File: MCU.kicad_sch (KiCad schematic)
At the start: 1 part, among them U1 STM32F030C8T6TR

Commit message: sch done open for review
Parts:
- added C10, C13, C14, C6, C7: 100nF, symbol Device:C_Small
- added C11, C12: 20pF, symbol Device:C_Small
- added C5: 4.7uF, symbol Device:C_Small
- added C8: 1uF, symbol Device:C_Small
- added C9: 10nF, symbol Device:C_Small
- added J2: SWD, symbol Connector:Conn_01x03_Pin
- added R2, R3, R4: 10K, symbol Device:R_Small
- added SW1, SW2, SW3: SW_SPST, symbol Switch:SW_SPST
- added Y1: 8MHZ, symbol Device:Crystal_Small
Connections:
- net VDDA is gone; now on net VCC_3v3: U1.9 (VDDA)
- net VDD__1 is gone; now on net VCC_3v3: U1.24 (VDD__1)
- net VDD__2 is gone; now on net VCC_3v3: U1.48 (VDD__2)
- net VSSA is gone; now on net GND: U1.8 (VSSA)
- net VSS__1 is gone; now on net GND: U1.47 (VSS__1)
- net BOOT0: now also R2.2
- net PA11: now also C13.2, R3.2, SW2.2 (B)
- net PA12: now also C14.2, R4.2, SW3.2 (B)
- net PA13_SWDIO: now also J2.3 (Pin_3)
- net PA14_SWCLK: now also J2.2 (Pin_2)
- net PF0-OSC_IN: now also C12.1, Y1.2
- net PF1-OSC_OUT: now also C11.1, Y1.1
- net ~{RST}: now also C10.2, SW1.2 (B)
- net PA15: no longer names the net of U1.38 (PA15)
- net PB3: no longer names the net of U1.39 (PB3)
- net PB4: no longer names the net of U1.40 (PB4)
- net PB5: no longer names the net of U1.41 (PB5)
- net PB6: no longer names the net of U1.42 (PB6)
- net PB7: no longer names the net of U1.43 (PB7)
- net PB8: no longer names the net of U1.45 (PB8)
- net PB9: no longer names the net of U1.46 (PB9)
- net PC13: no longer names the net of U1.2 (PC13)
- net PC14-OSC32_IN: no longer names the net of U1.3 (PC14-OSC32_IN)
- net PC15-OSC32_OUT: no longer names the net of U1.4 (PC15-OSC32_OUT)
- net PF6: no longer names the net of U1.35 (PF6)
- net PF7: no longer names the net of U1.36 (PF7)
- net VDD renamed VCC_3v3
- net VCC_3v3: now also C5.1, C6.1, C7.1, C8.1, C9.1, R3.1, R4.1
- net VSS renamed GND
- net GND: now also C10.1, C11.2, C12.2, C13.1, C14.1, C5.2, C6.2, C7.2, C8.2, C9.2, J2.1 (Pin_1), R2.1, SW1.1 (A), SW2.1 (A), SW3.1 (A)
- no-connect marks 0 -> 13
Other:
- title: (none) -> Nur-Al-Nujoom

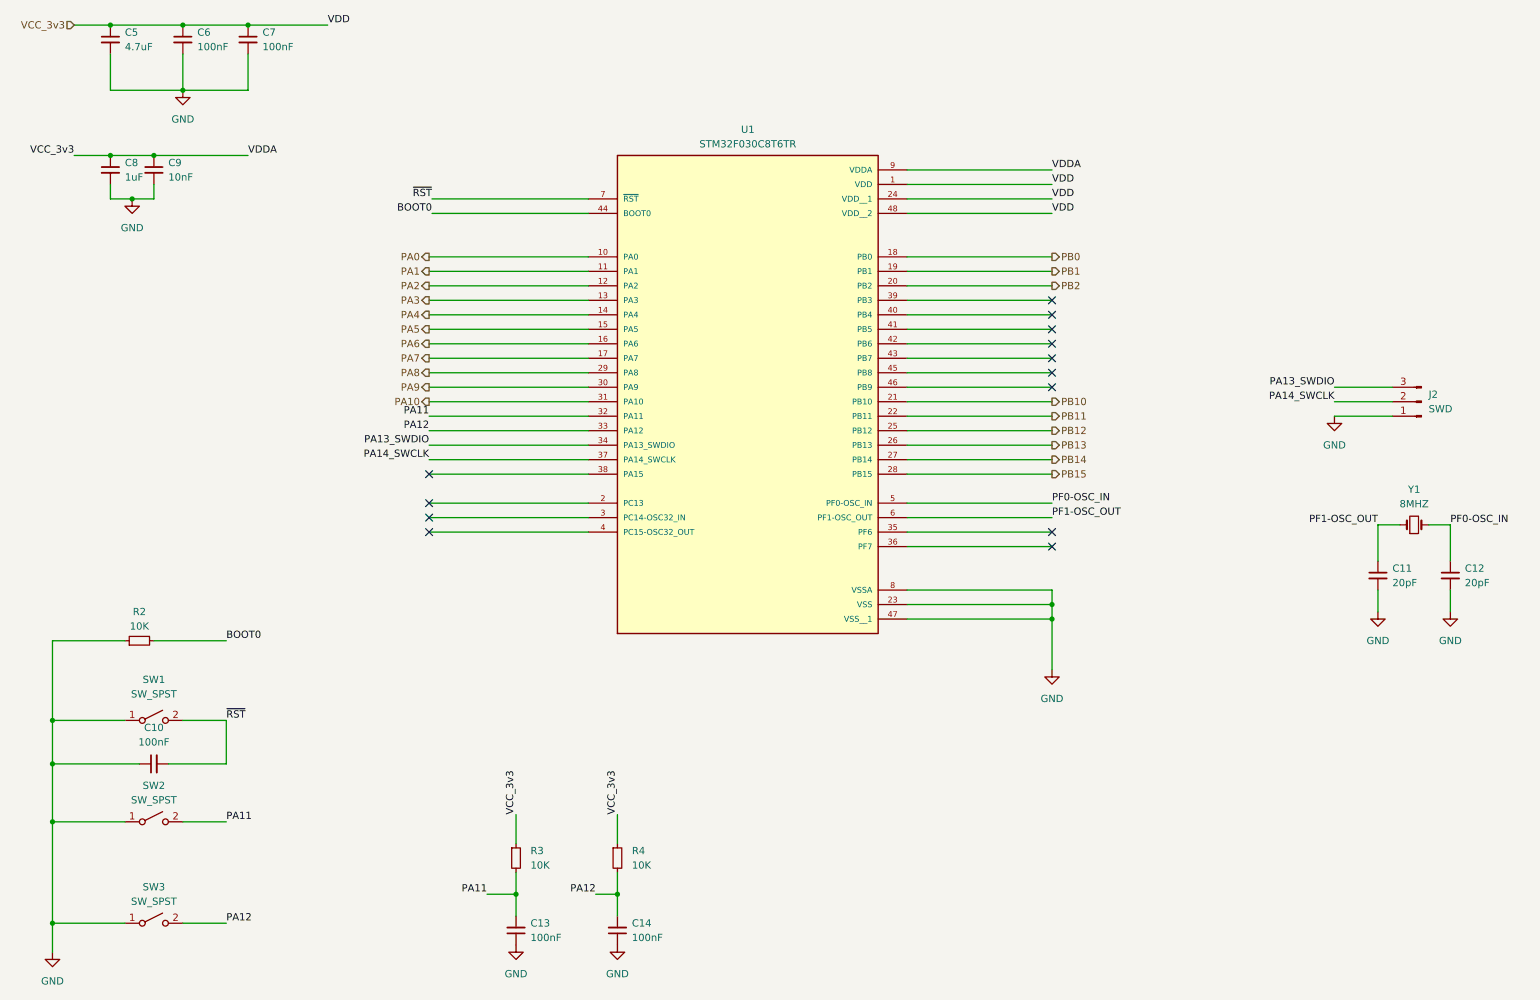
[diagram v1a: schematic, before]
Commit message: updated Routing
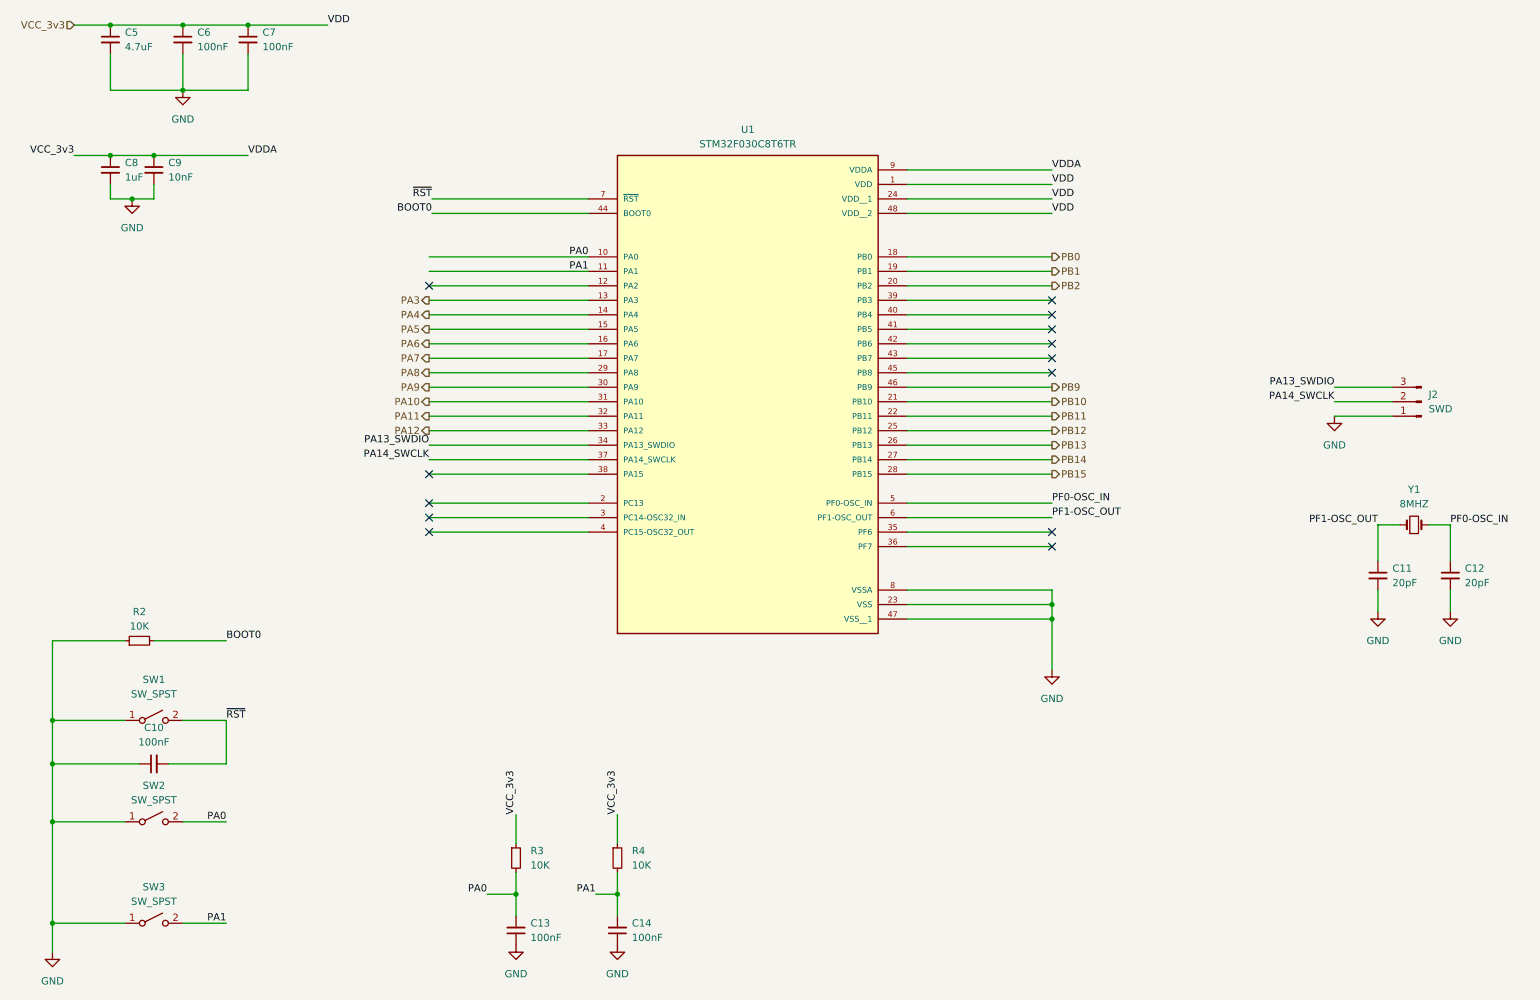
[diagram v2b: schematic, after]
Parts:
- C10, C11, C12, C13, C14, C5, C6, C7, C8, C9: footprint (none) -> Capacitor_SMD:C_0603_1608Metric
- J2: footprint (none) -> Connector_PinHeader_2.54mm:PinHeader_1x03_P2.54mm_Vertical
- R2, R3, R4: footprint (none) -> Resistor_SMD:R_0603_1608Metric
- SW1, SW2, SW3: footprint (none) -> Button_Switch_SMD:SW_SPST_CK_RS282G05A3
- Y1: footprint (none) -> Crystal:Crystal_SMD_HC49-SD
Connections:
- net PA0: now also C13.2, R3.2, SW2.2 (B)
- net PA1: now also C14.2, R4.2, SW3.2 (B)
- net PA11: no longer C13.2, R3.2, SW2.2 (B)
- net PA12: no longer C14.2, R4.2, SW3.2 (B)
- net PB9: now reaches U1.46 (PB9)
- net PA2: no longer names the net of U1.12 (PA2)
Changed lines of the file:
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@@
 	)
 	(no_connect
-		(at 196.85 110.49)
+		(at 87.63 67.31)
 	)
 	(no_connect
-		(at 196.85 80.01)
+		(at 196.85 110.49)
 	)
 	(no_connect
-		(at 196.85 85.09)
+		(at 196.85 80.01)
 	)
 	(no_connect
@@
 		)
 	)
-	(label "VDD"
-		(at 69.85 21.59 0)
-		(fields_autoplaced yes)
+	(label "PA0"
+		(at 115.57 62.23 180)
 		(effects
 			(font
 				(size 1.27 1.27)
 			)
-			(justify left bottom)
+			(justify right bottom)
 		)
 	)
-	(label "BOOT0"
-		(at 52.07 129.54 0)
+	(label "VDD"
+		(at 69.85 21.59 0)
 		(fields_autoplaced yes)
 		(effects
@@
 		)
 	)
-	(label "VDDA"
-		(at 55.88 44.45 0)
+	(label "BOOT0"
+		(at 52.07 129.54 0)
 		(fields_autoplaced yes)
 		(effects
@@
 		)
 	)
-	(label "PA11"
-		(at 52.07 161.29 0)
+	(label "VDDA"
+		(at 55.88 44.45 0)
 		(fields_autoplaced yes)
 		(effects
@@
 		)
 	)
-	(label "PA12"
-		(at 52.07 179.07 0)
-		(fields_autoplaced yes)
-		(effects
-			(font
-				(size 1.27 1.27)
-			)
-			(justify left bottom)
-		)
-	)
 	(label "VCC_3v3"
 		(at 25.4 44.45 180)
@@
 		)
 	)
+	(label "PA1"
+		(at 52.07 179.07 180)
+		(fields_autoplaced yes)
+		(effects
+			(font
+				(size 1.27 1.27)
+			)
+			(justify right bottom)
+		)
+	)
 	(label "VDD"
 		(at 196.85 54.61 0)
@@
 		)
 	)
-	(label "PA14_SWCLK"
-		(at 87.63 97.79 180)
+	(label "PA0"
+		(at 97.79 173.99 180)
 		(fields_autoplaced yes)
 		(effects
@@
 		)
 	)
-	(label "PF1-OSC_OUT"
-		(at 196.85 107.95 0)
+	(label "PA14_SWCLK"
+		(at 87.63 97.79 180)
 		(fields_autoplaced yes)
 		(effects
@@
 				(size 1.27 1.27)
 			)
-			(justify left bottom)
+			(justify right bottom)
 		)
 	)
-	(label "BOOT0"
-		(at 88.1379 54.61 180)
+	(label "PF1-OSC_OUT"
+		(at 196.85 107.95 0)
 		(fields_autoplaced yes)
 		(effects
@@
 				(size 1.27 1.27)
 			)
-			(justify right bottom)
+			(justify left bottom)
 		)
 	)
-	(label "PA12"
-		(at 116.84 173.99 180)
+	(label "BOOT0"
+		(at 88.1379 54.61 180)
 		(fields_autoplaced yes)
 		(effects
@@
 		)
 	)
-	(label "PA12"
-		(at 87.63 92.71 180)
+	(label "PA1"
+		(at 116.84 173.99 180)
 		(fields_autoplaced yes)
 		(effects
@@
 		)
 	)
-	(label "PA11"
-		(at 97.79 173.99 180)
+	(label "PA0"
+		(at 52.07 161.29 180)
 		(fields_autoplaced yes)
 		(effects
@@
 		)
 	)
-	(label "PA11"
-		(at 87.63 90.17 180)
-		(fields_autoplaced yes)
+	(label "PA1"
+		(at 115.57 64.77 180)
 		(effects
 			(font
@@
 		)
 	)
-	(hierarchical_label "PA2"
-		(shape output)
-		(at 87.63 67.31 180)
-		(fields_autoplaced yes)
-		(effects
-			(font
-				(size 1.27 1.27)
-			)
-			(justify right)
-		)
-	)
 	(hierarchical_label "PA3"
 		(shape output)
@@
 		)
 	)
-	(hierarchical_label "PA0"
+	(hierarchical_label "PA11"
 		(shape output)
-		(at 87.63 62.23 180)
+		(at 87.63 90.17 180)
 		(fields_autoplaced yes)
 		(effects
@@
 		)
 	)
-	(hierarchical_label "PA1"
+	(hierarchical_label "PA12"
 		(shape output)
-		(at 87.63 64.77 180)
+		(at 87.63 92.71 180)
 		(fields_autoplaced yes)
 		(effects
@@
 		)
 	)
+	(hierarchical_label "PB9"
+		(shape output)
+		(at 196.85 85.09 0)
+		(effects
+			(font
+				(size 1.27 1.27)
+			)
+			(justify left)
+		)
+	)
 	(hierarchical_label "PB15"
 		(shape output)
@@
 			)
 		)
-		(property "Footprint" ""
+		(property "Footprint" "Capacitor_SMD:C_0603_1608Metric"
 			(at 39.37 151.13 0)
 			(effects
@@
 			)
 		)
-		(property "Footprint" ""
+		(property "Footprint" "Resistor_SMD:R_0603_1608Metric"
 			(at 102.87 167.64 0)
 			(effects
@@
 			)
 		)
-		(property "Footprint" ""
+		(property "Footprint" "Button_Switch_SMD:SW_SPST_CK_RS282G05A3"
 			(at 39.37 179.07 0)
 			(effects
@@
 			)
 		)
-		(property "Footprint" ""
+		(property "Footprint" "Button_Switch_SMD:SW_SPST_CK_RS282G05A3"
 			(at 39.37 161.29 0)
 			(effects
@@
 			)
 		)
-		(property "Footprint" ""
+		(property "Footprint" "Crystal:Crystal_SMD_HC49-SD"
 			(at 260.35 109.22 0)
 			(effects
@@
 			)
 		)
-		(property "Footprint" ""
+		(property "Footprint" "Resistor_SMD:R_0603_1608Metric"
 			(at 120.65 167.64 0)
 			(effects
@@
 			)
 		)
-		(property "Footprint" ""
+		(property "Footprint" "Connector_PinHeader_2.54mm:PinHeader_1x03_P2.54mm_Vertical"
 			(at 261.62 87.63 0)
 			(effects
@@
 			)
 		)
-		(property "Footprint" ""
+		(property "Footprint" "Capacitor_SMD:C_0603_1608Metric"
 			(at 120.65 180.34 0)
 			(effects
@@
 			)
 		)
-		(property "Footprint" ""
+		(property "Footprint" "Capacitor_SMD:C_0603_1608Metric"
 			(at 44.45 24.13 0)
 			(effects
@@
 			)
 		)
-		(property "Footprint" ""
+		(property "Footprint" "Capacitor_SMD:C_0603_1608Metric"
 			(at 39.37 46.99 0)
 			(effects
@@
 			)
 		)
-		(property "Footprint" ""
+		(property "Footprint" "Button_Switch_SMD:SW_SPST_CK_RS282G05A3"
 			(at 39.37 143.51 0)
 			(effects
@@
 			)
 		)
-		(property "Footprint" ""
+		(property "Footprint" "Resistor_SMD:R_0603_1608Metric"
 			(at 36.83 129.54 0)
 			(effects
@@
 			)
 		)
-		(property "Footprint" ""
+		(property "Footprint" "Capacitor_SMD:C_0603_1608Metric"
 			(at 266.7 118.11 0)
 			(effects
@@
 			)
 		)
-		(property "Footprint" ""
+		(property "Footprint" "Capacitor_SMD:C_0603_1608Metric"
 			(at 31.75 46.99 0)
 			(effects
@@
 			)
 		)
-		(property "Footprint" ""
+		(property "Footprint" "Capacitor_SMD:C_0603_1608Metric"
 			(at 31.75 24.13 0)
 			(effects
@@
 			)
 		)
-		(property "Footprint" ""
+		(property "Footprint" "Capacitor_SMD:C_0603_1608Metric"
 			(at 55.88 24.13 0)
 			(effects
@@
 			)
 		)
-		(property "Footprint" ""
+		(property "Footprint" "Capacitor_SMD:C_0603_1608Metric"
 			(at 102.87 180.34 0)
 			(effects
@@
 			)
 		)
-		(property "Footprint" ""
+		(property "Footprint" "Capacitor_SMD:C_0603_1608Metric"
 			(at 254 118.11 0)
 			(effects
